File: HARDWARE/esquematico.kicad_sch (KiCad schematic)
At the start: 53 parts, among them J1 Screw_Terminal_01x02, J10 LCD I2C, J12 Screw_Terminal_01x02, J13 Screw_Terminal_01x02, J14 Screw_Terminal_01x02, J15 Screw_Terminal_01x02, J2 Screw_Terminal_01x02, J3 Screw_Terminal_01x02, J4 Screw_Terminal_01x02, J5 Screw_Terminal_01x02, J6 PINERA, K1 G6AU, K2 G6AU, K3 G6AU, K4 G6AU, Q1 2N7000, Q2 2N7000, Q3 2N7000, Q4 2N7000, SW1 SW_SPST, U1 PC817, U2 ESP32-DEVKITC-32D, U3 L7805, U4 PC817, U5 PC817, U6 PC817

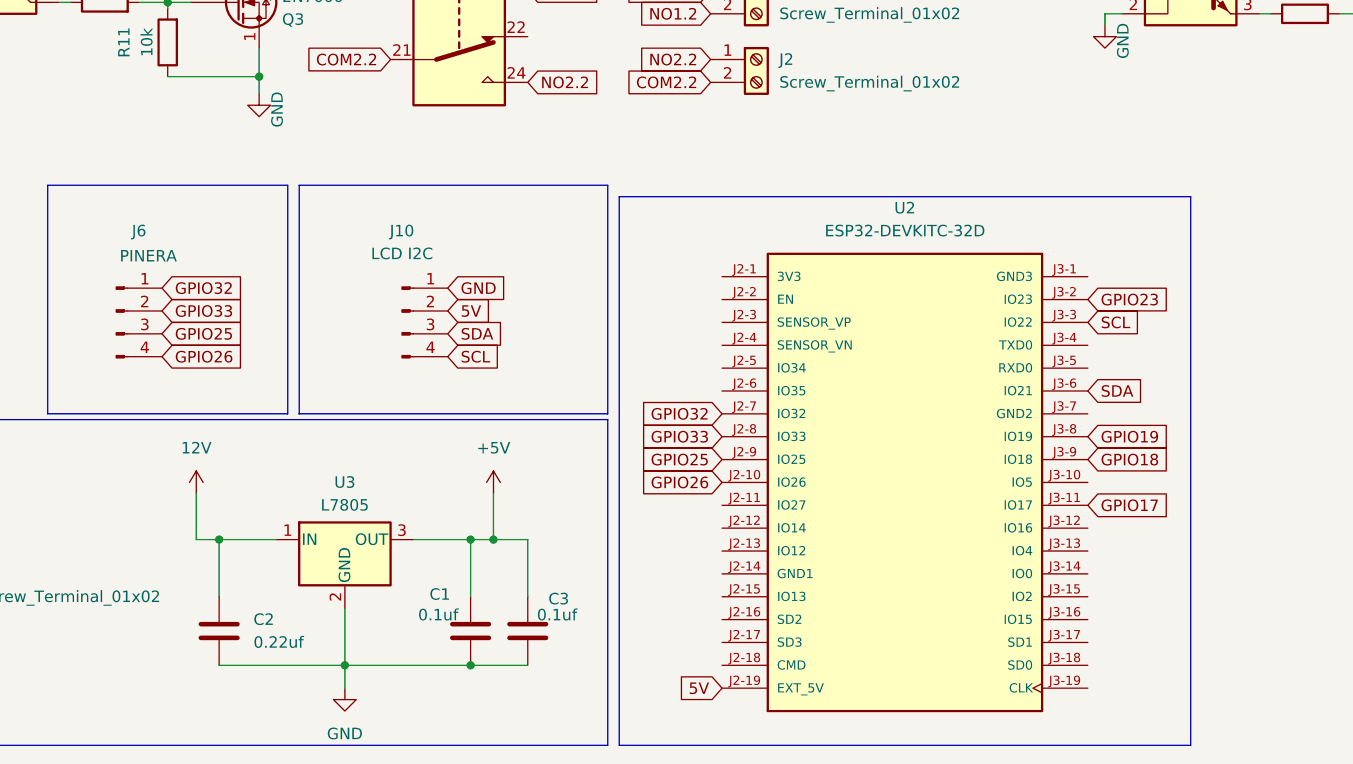
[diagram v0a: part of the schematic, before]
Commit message: cambie el esp32 de 38 pines por uno de 30
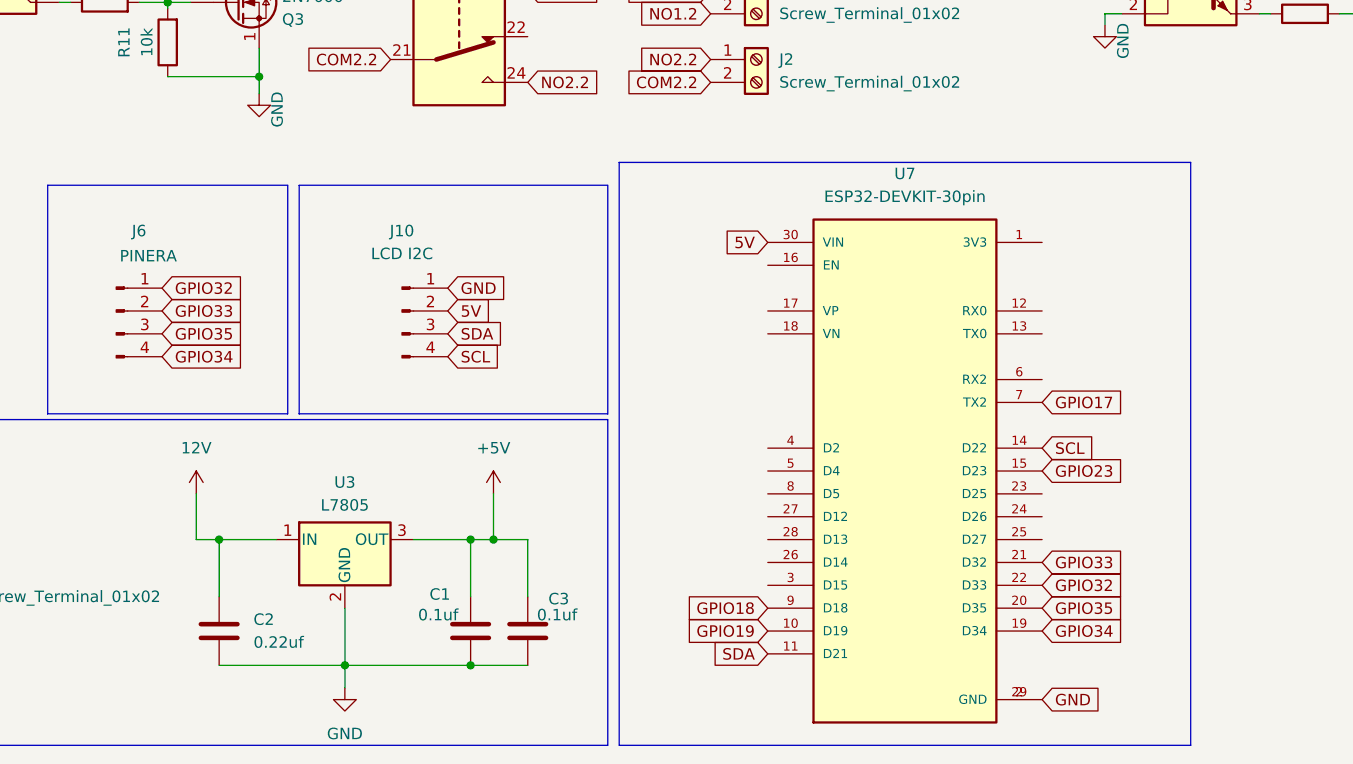
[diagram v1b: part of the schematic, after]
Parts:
- removed U2: ESP32-DEVKITC-32D, nueva huella esp32:MODULE_ESP32-DEVKITC-32D, symbol ESP32-DEVKITC-32D:ESP32-DEVKITC-32D
- added U7: ESP32-DEVKIT-30pin, MixLib-main:MODULE_ESP32_DEVKIT_V1, symbol MixLib:ESP32-DEVKIT-30pin
- J6: value PINERA -> PINERA
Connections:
- net 5V: now also U7.30 (VIN)
- net GND: now also U7.2 (GND), U7.29 (GND)
- net GPIO17: now also U7.7 (TX2)
- net GPIO18: now also U7.9 (D18)
- net GPIO19: now also U7.10 (D19)
- net GPIO23: now also U7.15 (D23)
- net GPIO32: now also U7.22 (D33)
- net GPIO33: now also U7.21 (D32)
- net SCL: now also U7.14 (D22)
- net SDA: now also U7.11 (D21)
- net GPIO25 renamed GPIO35
- net GPIO35: now also U7.20 (D35)
- net GPIO26 renamed GPIO34
- net GPIO34: now also U7.19 (D34)
